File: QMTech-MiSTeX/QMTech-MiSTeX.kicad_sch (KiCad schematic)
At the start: 18 parts, among them J1 RPi_GPIO, J10 Conn_01x06_Pin, J2 MiSTer SDRAM Module, J3 USB_C_Receptacle_USB2.0, J4 Conn_02x32_Odd_Even, J5 Conn_02x32_Odd_Even, J6 Conn_01x03_Pin, J9 Conn_01x03_Pin

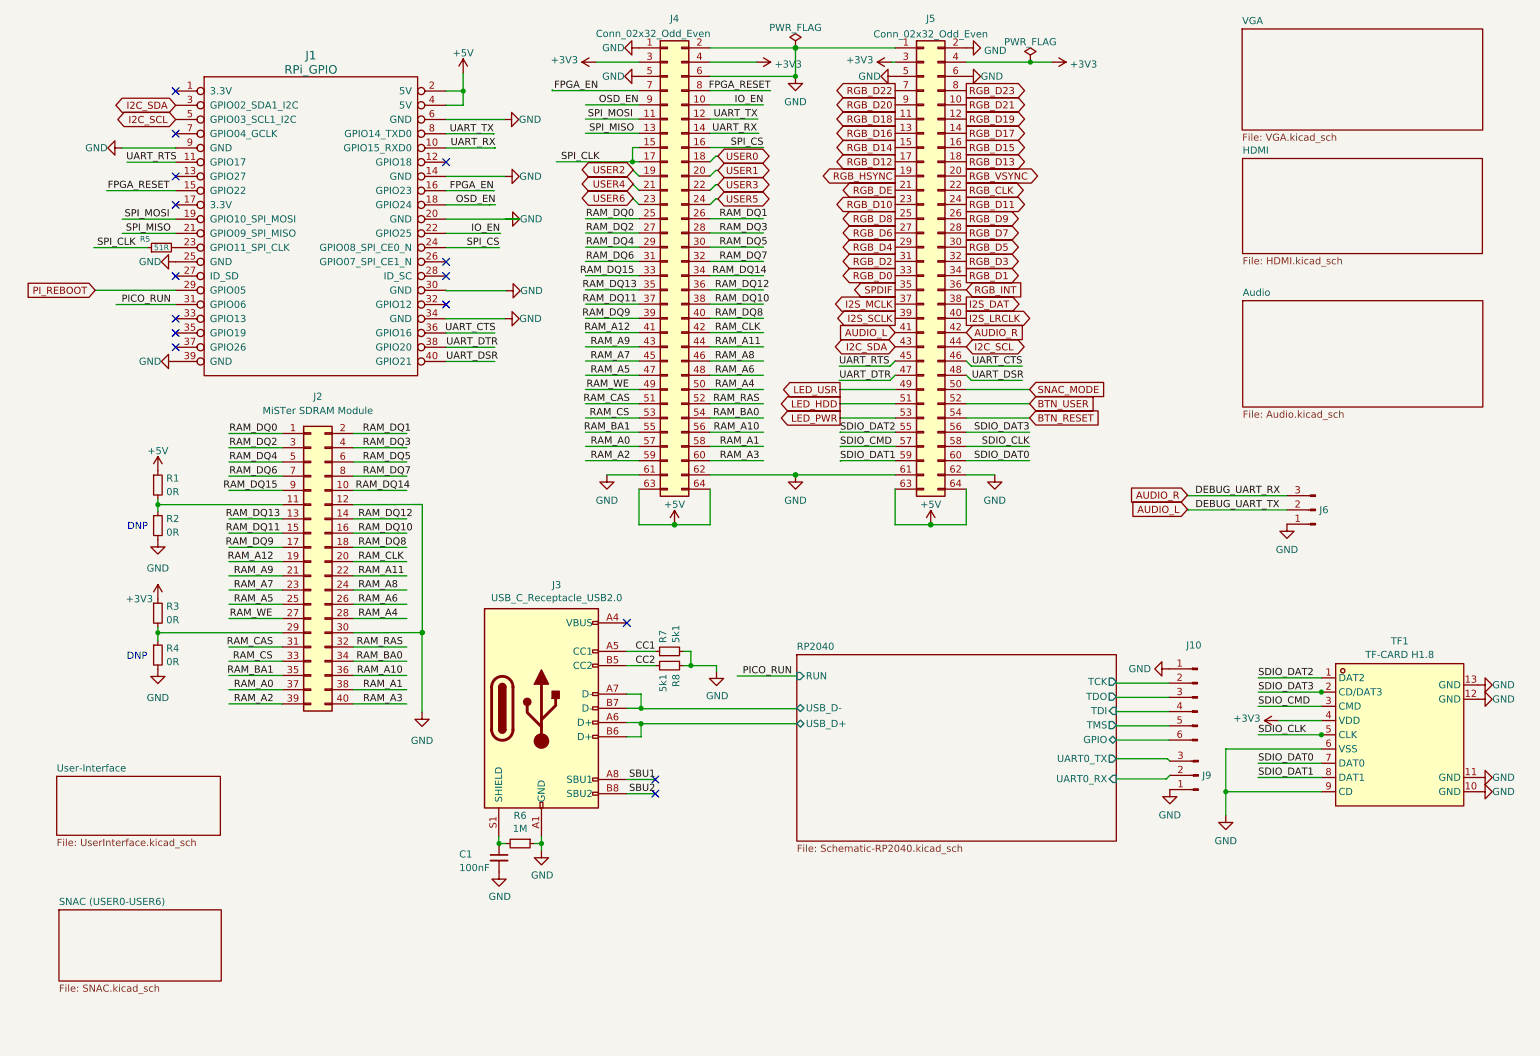
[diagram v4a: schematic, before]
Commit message: finish routing/layouting, fix silk screen, add mounting holes
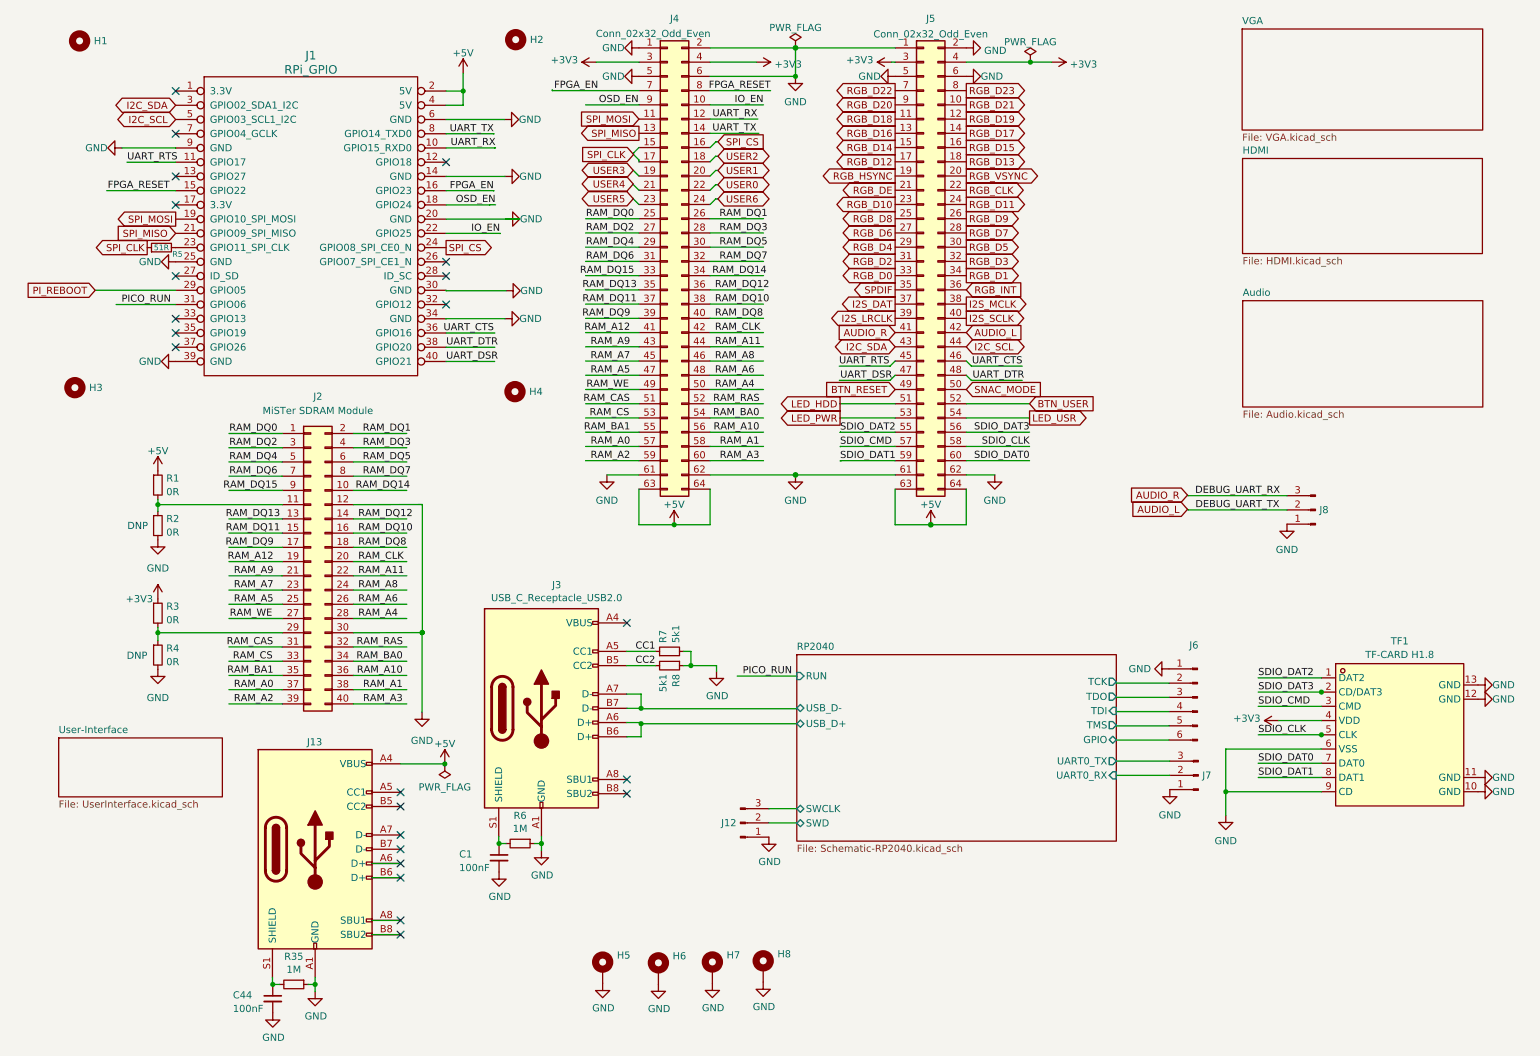
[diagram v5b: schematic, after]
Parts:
- added C44: 100nF, C_0402_1005Metric, symbol jlcpcb-basic-mlcc-0402:100nF
- added H1, H2, H3, H4: MountingHole, MountingHole:MountingHole_3mm, symbol Mechanical:MountingHole
- added H5, H6, H7, H8: MountingHole_Pad, MountingHole:MountingHole_3mm_Pad_Via, symbol Mechanical:MountingHole_Pad
- added J12: Conn_01x03_Pin, Connector_PinHeader_2.54mm:PinHeader_1x03_P2.54mm_Vertical, symbol Connector:Conn_01x03_Pin
- added J13: USB_C_Receptacle_USB2.0, Connector_USB:USB_C_Receptacle_XKB_U262-16XN-4BVC11, symbol PmodUsbUlpi-rescue:USB_C_Receptacle_USB2.0-Connector
- added R35: 1M, Resistor_SMD:R_0603_1608Metric, symbol Device:R_Small
- J1: footprint Connector_PinSocket_2.54mm:PinSocket_2x20_P2.54mm_Vertical -> Connector_PinHeader_2.54mm:PinHeader_2x20_P2.54mm_Vertical
- renumbered J10 to J6, J9 to J7, J6 to J8
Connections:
- net +5V: now also J13.A4 (VBUS), J13.A9 (VBUS), J13.B4 (VBUS), J13.B9 (VBUS)
- net AUDIO_L: now also J5.42 (Pin_42); no longer J5.41 (Pin_41)
- net AUDIO_R: now also J5.41 (Pin_41); no longer J5.42 (Pin_42)
- net BTN_RESET: now also J5.49 (Pin_49); no longer J5.54 (Pin_54)
- net GND: now also C44.2, H5.1, H6.1, H7.1, H8.1, J12.1 (Pin_1), J13.A1 (GND), J13.A12 (GND), J13.B1 (GND), J13.B12 (GND), R35.1
- net I2S_DAT: now also J5.37 (Pin_37); no longer J5.38 (Pin_38)
- net I2S_LRCLK: now also J5.39 (Pin_39); no longer J5.40 (Pin_40)
- net I2S_MCLK: now also J5.38 (Pin_38); no longer J5.37 (Pin_37)
- net I2S_SCLK: now also J5.40 (Pin_40); no longer J5.39 (Pin_39)
- net LED_USR: now also J5.54 (Pin_54); no longer J5.49 (Pin_49)
- net UART_CTS: now also J1.36 (GPIO16)
- net UART_DSR: now also J5.47 (Pin_47); no longer J5.48 (Pin_48)
- net UART_DTR: now also J5.48 (Pin_48); no longer J5.47 (Pin_47)
- net UART_RTS: now also J1.11 (GPIO17)
- net UART_RX: now also J4.12 (Pin_12); no longer J4.14 (Pin_14)
- net UART_TX: now also J4.14 (Pin_14); no longer J4.12 (Pin_12)
- net USER0: now also J4.22 (Pin_22); no longer J4.18 (Pin_18)
- net USER2: now also J4.18 (Pin_18); no longer J4.19 (Pin_19)
- net USER3: now also J4.19 (Pin_19); no longer J4.22 (Pin_22)
- net USER5: now also J4.23 (Pin_23); no longer J4.24 (Pin_24)
- net USER6: now also J4.24 (Pin_24); no longer J4.23 (Pin_23)
- net SBU1: no longer names the net of J3.A8 (SBU1)
- net SBU2: no longer names the net of J3.B8 (SBU2)
- new net: C44.1, J13.S1 (SHIELD), R35.2
- new net RP2040/SWCLK: J12.3 (Pin_3)
- new net RP2040/SWD: J12.2 (Pin_2)
- no-connect marks 15 -> 23
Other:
- removed sheet SNAC (USER0-USER6)
- sheet RP2040 ports: added SWCLK, SWD; removed none

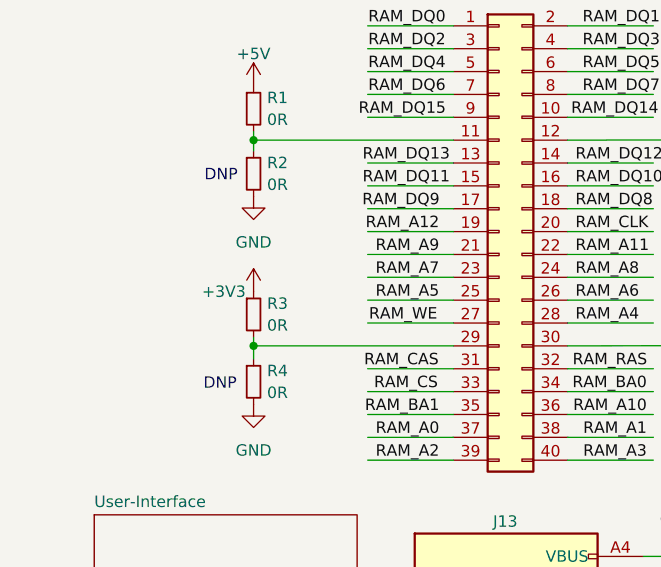
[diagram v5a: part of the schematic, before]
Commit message: fix DRC errors and some warnings too
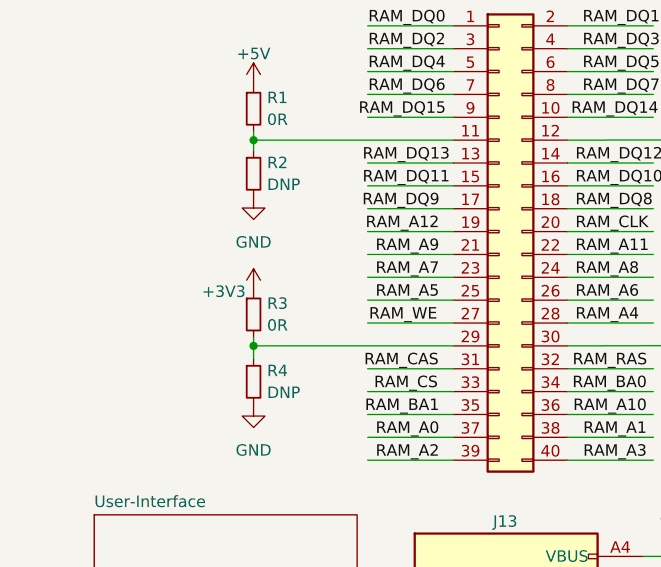
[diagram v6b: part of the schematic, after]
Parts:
- R2, R4: value 0R -> DNP
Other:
- note removed: "DNP"
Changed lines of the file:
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@@
     )
-  )
-  (text "DNP" (at 32.258 105.283 0)
-    (effects (font (size 1.27 1.27)) (justify left bottom))
-  )
-  (text "DNP" (at 32.1497 128.4478 0)
-    (effects (font (size 1.27 1.27)) (justify left bottom))
   )
   (label "RAM_DQ13" (at 59.5333 103.0732 180) (fields_autoplaced)
@@
       (effects (font (size 1.27 1.27)) (justify left))
     )
-    (property "Value" "0R" (at 39.2176 128.5931 0)
+    (property "Value" "DNP" (at 39.2176 128.5931 0)
       (effects (font (size 1.27 1.27)) (justify left))
     )
@@
       (effects (font (size 1.27 1.27)) (justify left))
     )
-    (property "Value" "0R" (at 39.2176 105.4791 0)
-      (effects (font (size 1.27 1.27)) (justify left))
-    )
+    (property "Value" "DNP" (at 39.2176 105.4791 0)
+      (effects (font (size 1.27 1.27)) (justify left))
+    )

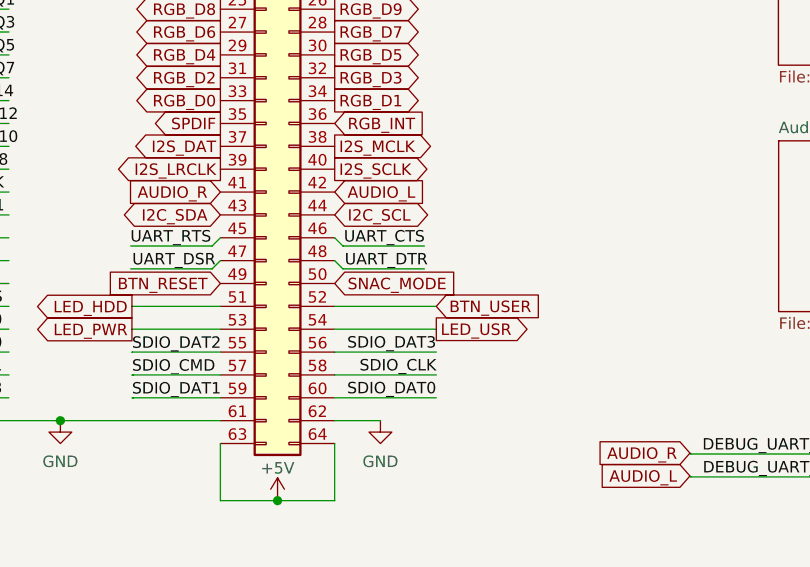
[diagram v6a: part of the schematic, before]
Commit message: get rid of SNAC mode switch and add OSD button instead
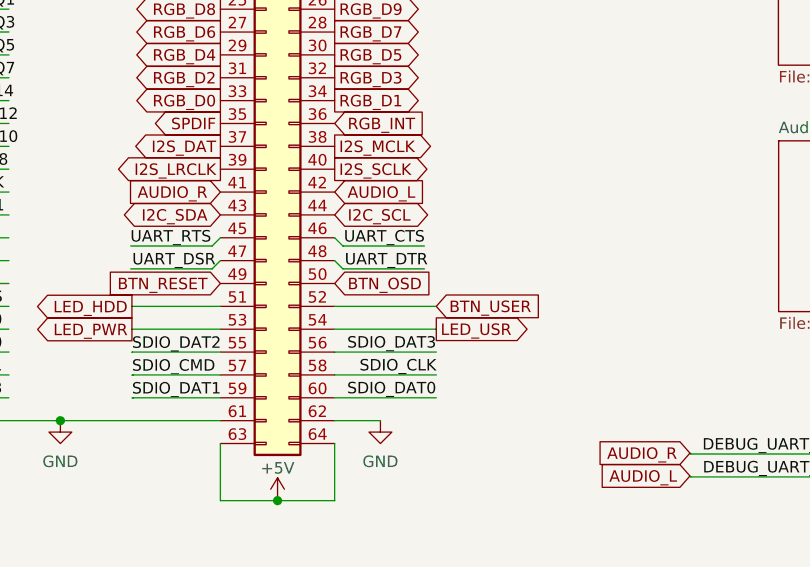
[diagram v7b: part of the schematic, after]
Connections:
- net SNAC_MODE renamed BTN_OSD
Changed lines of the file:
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@@
     (effects (font (size 1.27 1.27)) (justify right bottom))
   )
-  (global_label "SNAC_MODE" (shape input) (at 181.991 79.9846 0) (fields_autoplaced)
+  (global_label "BTN_OSD" (shape input) (at 181.991 79.9846 0) (fields_autoplaced)
     (effects (font (size 1.27 1.27)) (justify left))
-    (property "Intersheetrefs" "${INTERSHEET_REFS}" (at 196.0433 79.9846 0)
+    (property "Intersheetrefs" "${INTERSHEET_REFS}" (at 193.417 79.9846 0)
       (effects (font (size 1.27 1.27)) (justify left))
     )
